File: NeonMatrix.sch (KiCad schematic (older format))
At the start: 0 parts

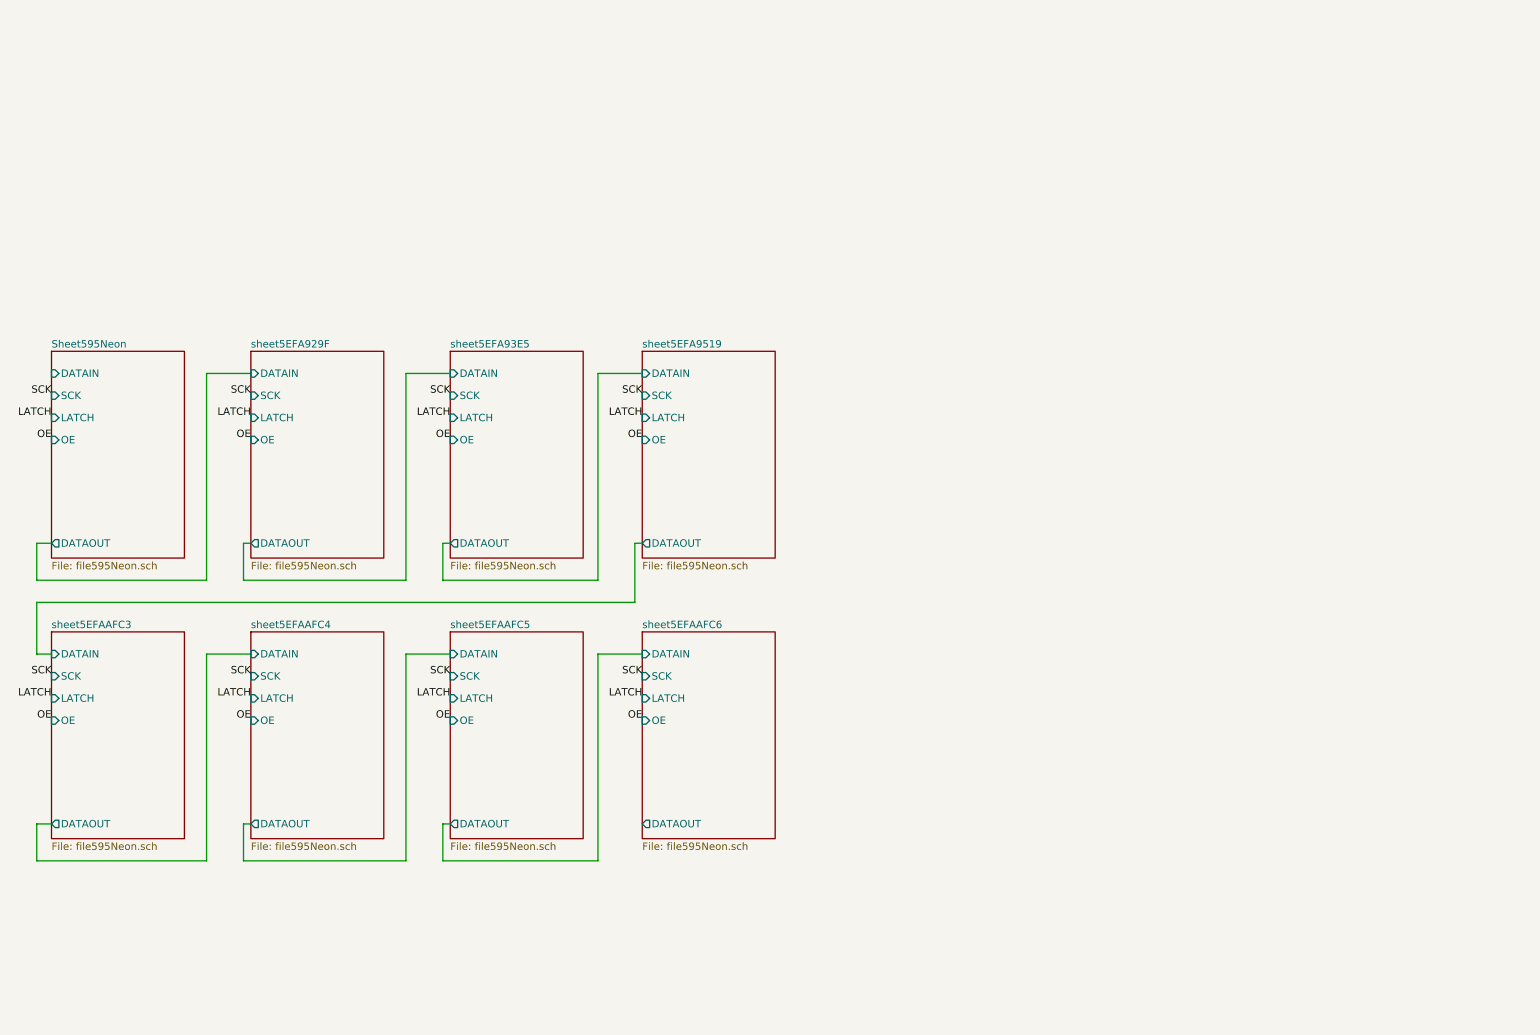
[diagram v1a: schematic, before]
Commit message: Add isolation
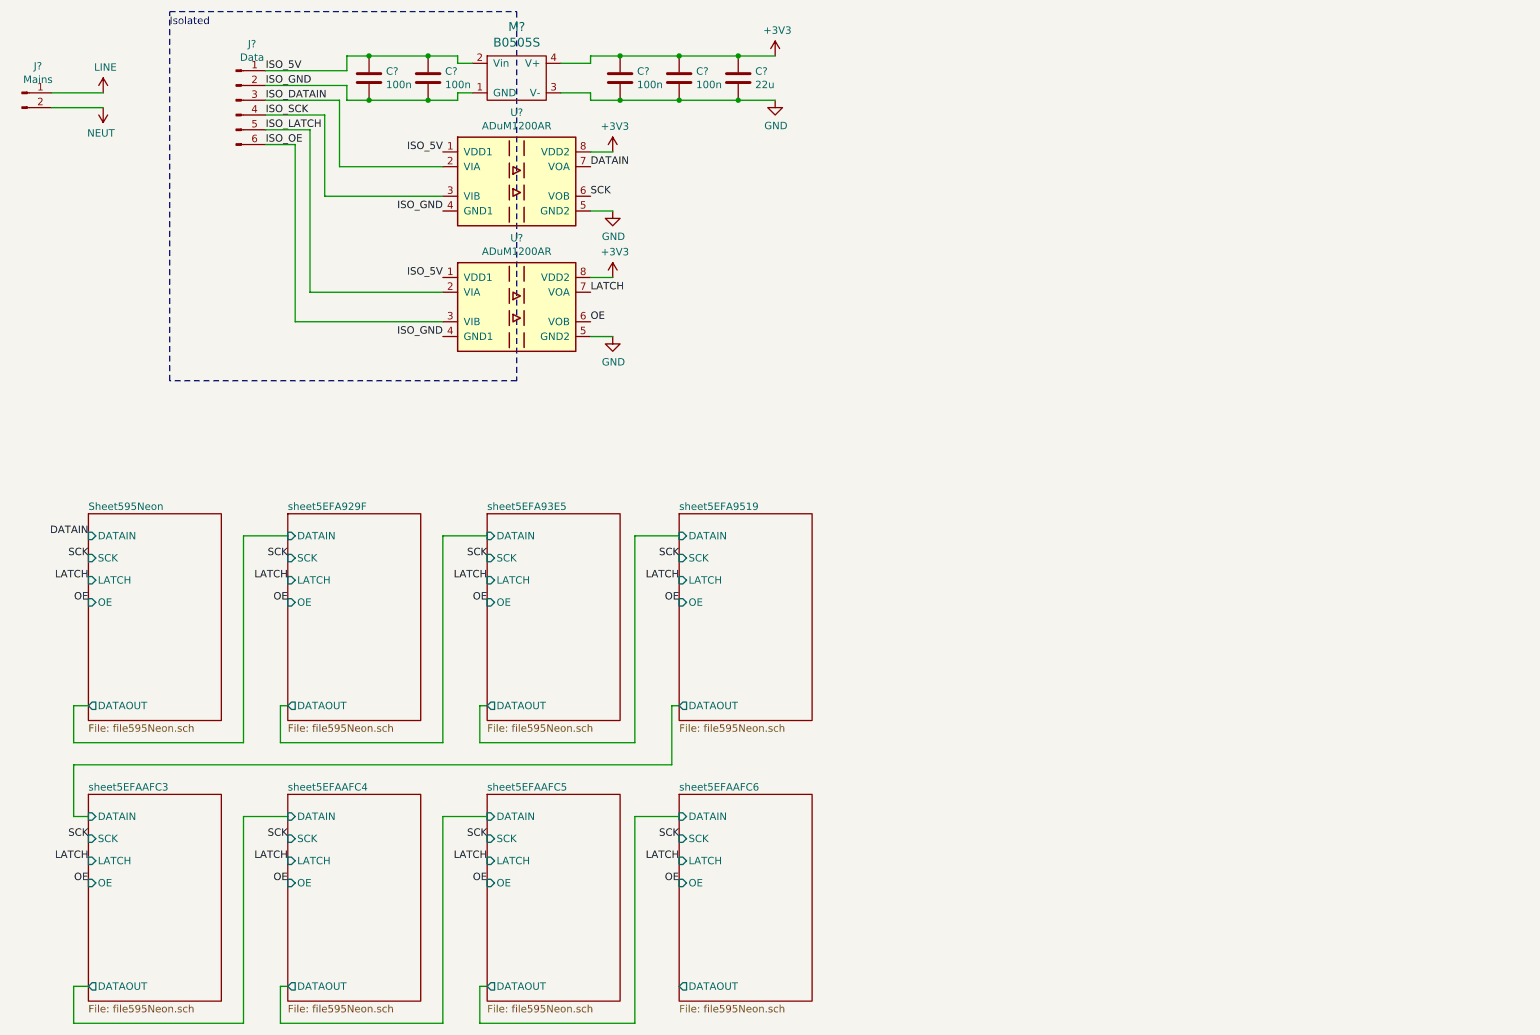
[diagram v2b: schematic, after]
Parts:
- added C? (x4): 100n, Capacitor_SMD:C_0805_2012Metric, symbol Device:C
- added C?: 22u, Capacitor_SMD:C_0805_2012Metric, symbol Device:C
- added J?: Mains, TerminalBlock_RND:TerminalBlock_RND_205-00001_1x02_P5.00mm_Horizontal, symbol Connector:Conn_01x02_Male
- added J?: Data, Connector_PinHeader_2.54mm:PinHeader_1x06_P2.54mm_Vertical, symbol Connector:Conn_01x06_Male
- added M?: B0505S, NeonMatrix:M_DCDC_SIP4, symbol NeonMatrix:B0505S
- added U? (x2): ADuM1200AR, Package_SO:SOIC-8_3.9x4.9mm_P1.27mm, symbol Isolator:ADuM1200AR
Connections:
- net LATCH: now also U?.7 (VOA)
- net OE: now also U?.6 (VOB)
- net SCK: now also U?.6 (VOB)
- new net +3V3: C?.1, C?.1, C?.1, M?.4 (V+), U?.8 (VDD2), U?.8 (VDD2)
- new net DATAIN: U?.7 (VOA)
- new net GND: C?.2, C?.2, C?.2, M?.3 (V-), U?.5 (GND2), U?.5 (GND2)
- new net ISO_5V: C?.1, C?.1, J?.1 (Pin_1), M?.2 (Vin), U?.1 (VDD1), U?.1 (VDD1)
- new net ISO_DATAIN: J?.3 (Pin_3), U?.2 (VIA)
- new net ISO_GND: C?.2, C?.2, J?.2 (Pin_2), M?.1 (GND), U?.4 (GND1), U?.4 (GND1)
- new net ISO_LATCH: J?.5 (Pin_5), U?.2 (VIA)
- new net ISO_OE: J?.6 (Pin_6), U?.3 (VIB)
- new net ISO_SCK: J?.4 (Pin_4), U?.3 (VIB)
- new net LINE: J?.1 (Pin_1)
- new net NEUT: J?.2 (Pin_2)
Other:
- note added: "Isolated"

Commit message: Add routing
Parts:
- gave numbers to parts that had none: 10
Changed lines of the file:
@@
 	1200 6050 1300 6050
 $Comp
-L Connector:Conn_01x02_Male J?
+L Connector:Conn_01x02_Male J1
 U 1 1 5EF252E6
 P 850 1150
-F 0 "J?" H 958 1331 50  0000 C CNN
+F 0 "J1" H 958 1331 50  0000 C CNN
 F 1 "Mains" H 958 1240 50  0000 C CNN
 F 2 "TerminalBlock_RND:TerminalBlock_RND_205-00001_1x02_P5.00mm_Horizontal" H 850 1150 50  0001 C CNN
@@
 $EndComp
 $Comp
-L power:LINE #PWR?
+L power:LINE #PWR0269
 U 1 1 5EF25E29
 P 1400 1150
-F 0 "#PWR?" H 1400 1000 50  0001 C CNN
+F 0 "#PWR0269" H 1400 1000 50  0001 C CNN
 F 1 "LINE" H 1415 1323 50  0000 C CNN
 F 2 "" H 1400 1150 50  0001 C CNN
@@
 $EndComp
 $Comp
-L power:NEUT #PWR?
+L power:NEUT #PWR0270
 U 1 1 5EF26410
 P 1400 1250
-F 0 "#PWR?" H 1400 1100 50  0001 C CNN
+F 0 "#PWR0270" H 1400 1100 50  0001 C CNN
 F 1 "NEUT" H 1415 1423 50  0000 C CNN
 F 2 "" H 1400 1250 50  0001 C CNN
@@
 	1400 1250 1050 1250
 $Comp
-L Connector:Conn_01x06_Male J?
+L Connector:Conn_01x06_Male J2
 U 1 1 5EF289F0
 P 2300 1200
-F 0 "J?" H 2408 1581 50  0000 C CNN
+F 0 "J2" H 2408 1581 50  0000 C CNN
 F 1 "Data" H 2408 1490 50  0000 C CNN
 F 2 "Connector_PinHeader_2.54mm:PinHeader_1x06_P2.54mm_Vertical" H 2300 1200 50  0001 C CNN
@@
 $EndComp
 $Comp
-L NeonMatrix:B0505S M?
+L NeonMatrix:B0505S M1
 U 1 1 5EF2D5C5
 P 4200 1050
-F 0 "M?" H 4200 1397 60  0000 C CNN
+F 0 "M1" H 4200 1397 60  0000 C CNN
 F 1 "B0505S" H 4200 1291 60  0000 C CNN
 F 2 "NeonMatrix:M_DCDC_SIP4" H 4200 1050 60  0001 C CNN
@@
 	2500 1100 3050 1100
 $Comp
-L Isolator:ADuM1200AR U?
+L Isolator:ADuM1200AR U9
 U 1 1 5EF33638
 P 4200 1750
-F 0 "U?" H 4200 2217 50  0000 C CNN
+F 0 "U9" H 4200 2217 50  0000 C CNN
 F 1 "ADuM1200AR" H 4200 2126 50  0000 C CNN
 F 2 "Package_SO:SOIC-8_3.9x4.9mm_P1.27mm" H 4200 1350 50  0001 C CIN
@@
 $EndComp
 $Comp
-L Isolator:ADuM1200AR U?
+L Isolator:ADuM1200AR U10
 U 1 1 5EF3D01E
 P 4200 2600
-F 0 "U?" H 4200 3067 50  0000 C CNN
+F 0 "U10" H 4200 3067 50  0000 C CNN
 F 1 "ADuM1200AR" H 4200 2976 50  0000 C CNN
 F 2 "Package_SO:SOIC-8_3.9x4.9mm_P1.27mm" H 4200 2200 50  0001 C CIN
@@
 ISO_OE
 $Comp
-L power:+3V3 #PWR?
+L power:+3V3 #PWR0271
 U 1 1 5EF5670B
 P 5950 900
-F 0 "#PWR?" H 5950 750 50  0001 C CNN
+F 0 "#PWR0271" H 5950 750 50  0001 C CNN
 F 1 "+3V3" H 5965 1073 50  0000 C CNN
 F 2 "" H 5950 900 50  0001 C CNN
@@
 $EndComp
 $Comp
-L power:GND #PWR?
+L power:GND #PWR0272
 U 1 1 5EF56B42
 P 5950 1200
-F 0 "#PWR?" H 5950 950 50  0001 C CNN
+F 0 "#PWR0272" H 5950 950 50  0001 C CNN
 F 1 "GND" H 5955 1027 50  0000 C CNN
 F 2 "" H 5950 1200 50  0001 C CNN
@@
 $EndComp
 $Comp
-L Device:C C?
+L Device:C C1
 U 1 1 5EF5D2D3
 P 3200 1050
-F 0 "C?" H 3315 1096 50  0000 L CNN
+F 0 "C1" H 3315 1096 50  0000 L CNN
 F 1 "100n" H 3315 1005 50  0000 L CNN
 F 2 "Capacitor_SMD:C_0805_2012Metric" H 3238 900 50  0001 C CNN
@@
 $EndComp
 $Comp
-L Device:C C?
+L Device:C C2
 U 1 1 5EF5E43E
 P 3600 1050
-F 0 "C?" H 3715 1096 50  0000 L CNN
+F 0 "C2" H 3715 1096 50  0000 L CNN
 F 1 "100n" H 3715 1005 50  0000 L CNN
 F 2 "Capacitor_SMD:C_0805_2012Metric" H 3638 900 50  0001 C CNN
@@
 $EndComp
 $Comp
-L Device:C C?
+L Device:C C3
 U 1 1 5EF60A70
 P 4900 1050
-F 0 "C?" H 5015 1096 50  0000 L CNN
+F 0 "C3" H 5015 1096 50  0000 L CNN
 F 1 "100n" H 5015 1005 50  0000 L CNN
 F 2 "Capacitor_SMD:C_0805_2012Metric" H 4938 900 50  0001 C CNN
@@
 	4700 900  4900 900
 $Comp
-L power:+3V3 #PWR?
+L power:+3V3 #PWR0273
 U 1 1 5EF80809
 P 4850 1550
-F 0 "#PWR?" H 4850 1400 50  0001 C CNN
+F 0 "#PWR0273" H 4850 1400 50  0001 C CNN
 F 1 "+3V3" H 4865 1723 50  0000 C CNN
 F 2 "" H 4850 1550 50  0001 C CNN
@@
 $EndComp
 $Comp
-L power:+3V3 #PWR?
+L power:+3V3 #PWR0274
 U 1 1 5EF80E8F
 P 4850 2400
-F 0 "#PWR?" H 4850 2250 50  0001 C CNN
+F 0 "#PWR0274" H 4850 2250 50  0001 C CNN
 F 1 "+3V3" H 4865 2573 50  0000 C CNN
 F 2 "" H 4850 2400 50  0001 C CNN
@@
 $EndComp
 $Comp
-L Device:C C?
+L Device:C C4
 U 1 1 5EF888A6
 P 5300 1050
-F 0 "C?" H 5415 1096 50  0000 L CNN
+F 0 "C4" H 5415 1096 50  0000 L CNN
 F 1 "100n" H 5415 1005 50  0000 L CNN
 F 2 "Capacitor_SMD:C_0805_2012Metric" H 5338 900 50  0001 C CNN
@@
 	5300 1200 5700 1200
 $Comp
-L power:GND #PWR?
+L power:GND #PWR0275
 U 1 1 5EF8F4F0
 P 4850 2800
-F 0 "#PWR?" H 4850 2550 50  0001 C CNN
+F 0 "#PWR0275" H 4850 2550 50  0001 C CNN
 F 1 "GND" H 4855 2627 50  0000 C CNN
 F 2 "" H 4850 2800 50  0001 C CNN
@@
 $EndComp
 $Comp
-L power:GND #PWR?
+L power:GND #PWR0276
 U 1 1 5EF90F2B
 P 4850 1950
-F 0 "#PWR?" H 4850 1700 50  0001 C CNN
+F 0 "#PWR0276" H 4850 1700 50  0001 C CNN
 F 1 "GND" H 4855 1777 50  0000 C CNN
 F 2 "" H 4850 1950 50  0001 C CNN
@@
 OE
 $Comp
-L Device:C C?
+L Device:C C5
 U 1 1 5EFA144C
 P 5700 1050
-F 0 "C?" H 5815 1096 50  0000 L CNN
+F 0 "C5" H 5815 1096 50  0000 L CNN
 F 1 "22u" H 5815 1005 50  0000 L CNN
 F 2 "Capacitor_SMD:C_0805_2012Metric" H 5738 900 50  0001 C CNN

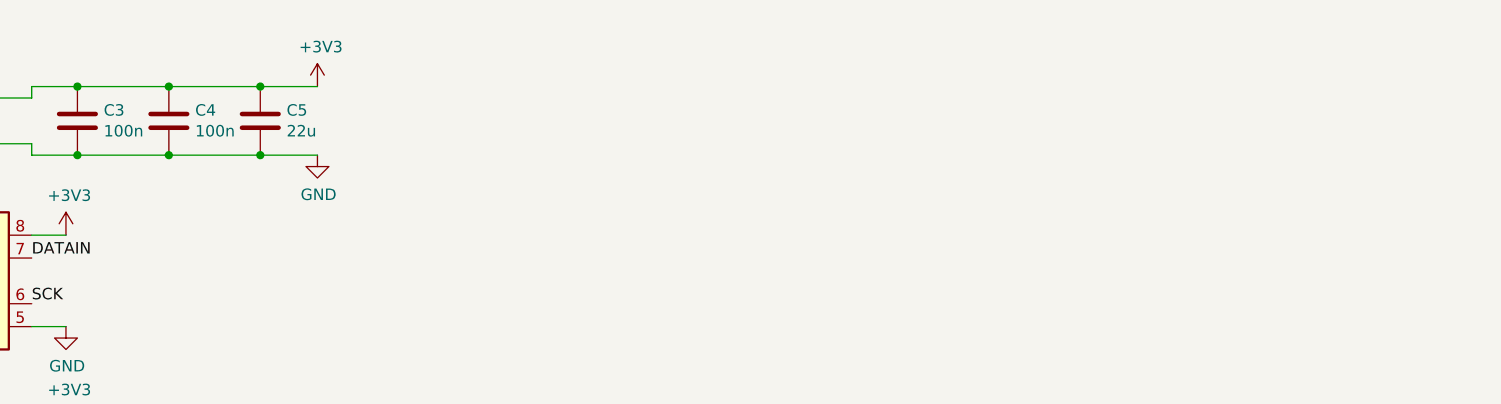
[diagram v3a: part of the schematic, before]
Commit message: Add PCB markings
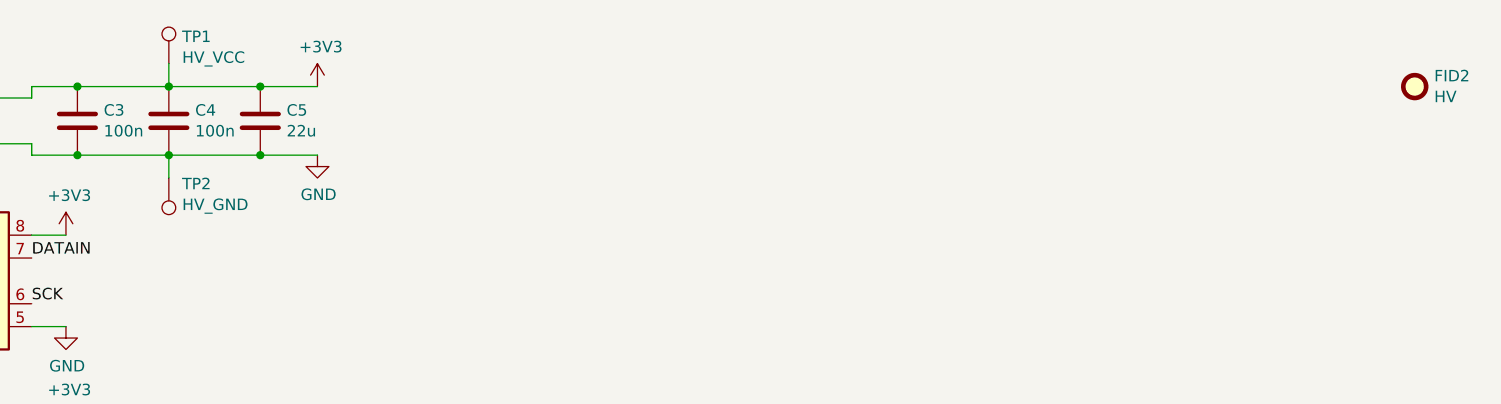
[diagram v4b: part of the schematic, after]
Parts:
- added FID2: HV, Symbol:Symbol_HighVoltage_Type1_CopperTop_Big, symbol Mechanical:Fiducial
- added TP1: HV_VCC, TestPoint:TestPoint_Pad_2.0x2.0mm, symbol Connector:TestPoint
- added TP2: HV_GND, TestPoint:TestPoint_Pad_2.0x2.0mm, symbol Connector:TestPoint
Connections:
- net +3V3: now also TP1.1
- net GND: now also TP2.1
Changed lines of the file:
@@
 Wire Wire Line
 	4500 950  4700 950
-Wire Wire Line
-	4700 900  4900 900
 $Comp
 L power:+3V3 #PWR0273
@@
 Wire Wire Line
 	5700 1200 5950 1200
+$Comp
+L Mechanical:Fiducial FID2
+U 1 1 5EF2A5C0
+P 10750 900
+F 0 "FID2" H 10835 946 50  0000 L CNN
+F 1 "HV" H 10835 855 50  0000 L CNN
+F 2 "Symbol:Symbol_HighVoltage_Type1_CopperTop_Big" H 10750 900 50  0001 C CNN
+F 3 "~" H 10750 900 50  0001 C CNN
+	1    10750 900
+	1    0    0    -1
+$EndComp
+$Comp
+L Connector:TestPoint TP1
+U 1 1 5EF2C852
+P 5300 800
+F 0 "TP1" H 5358 918 50  0000 L CNN
+F 1 "HV_VCC" H 5358 827 50  0000 L CNN
+F 2 "TestPoint:TestPoint_Pad_2.0x2.0mm" H 5500 800 50  0001 C CNN
+F 3 "~" H 5500 800 50  0001 C CNN
+	1    5300 800
+	1    0    0    -1
+$EndComp
+$Comp
+L Connector:TestPoint TP2
+U 1 1 5EF39EDF
+P 5300 1300
+F 0 "TP2" H 5242 1326 50  0000 R CNN
+F 1 "HV_GND" H 5242 1417 50  0000 R CNN
+F 2 "TestPoint:TestPoint_Pad_2.0x2.0mm" H 5500 1300 50  0001 C CNN
+F 3 "~" H 5500 1300 50  0001 C CNN
+	1    5300 1300
+	-1   0    0    1
+$EndComp
+Wire Wire Line
+	4700 900  4900 900
+Wire Wire Line
+	5300 800  5300 900
+Wire Wire Line
+	5300 1300 5300 1200
 $EndSCHEMATC

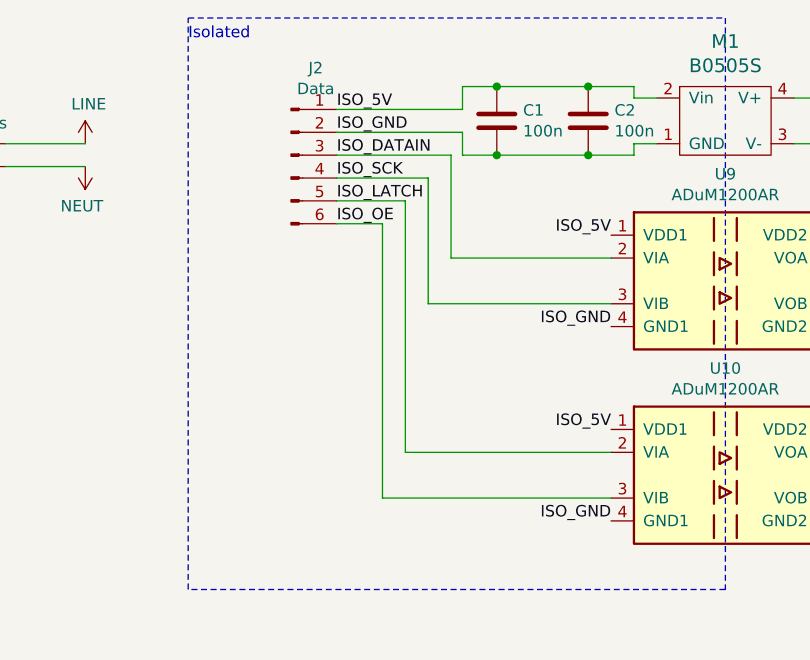
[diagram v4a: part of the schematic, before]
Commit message: Add bulk capacitance, fix isolation, silkscreen and vias
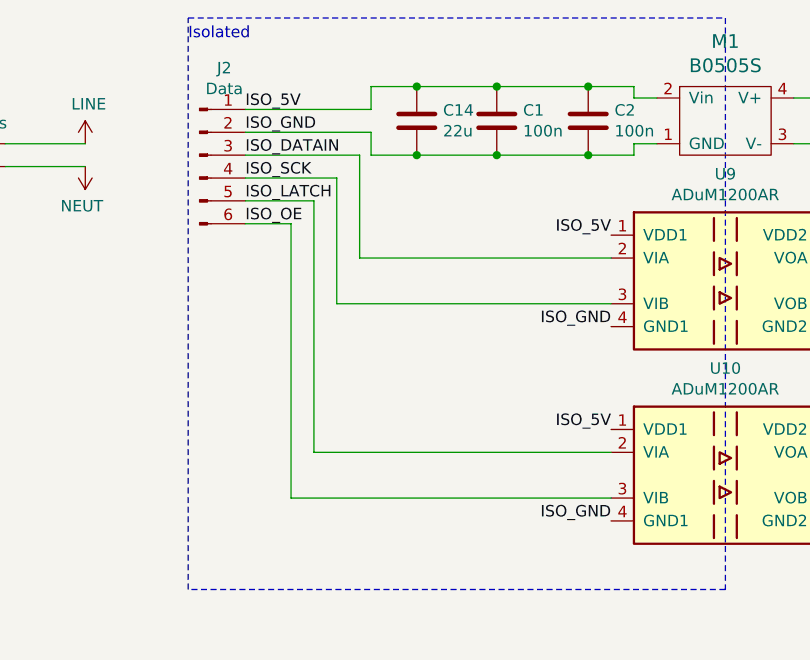
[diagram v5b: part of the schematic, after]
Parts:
- added C14: 22u, Capacitor_SMD:C_0805_2012Metric, symbol Device:C
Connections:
- net ISO_5V: now also C14.1
- net ISO_GND: now also C14.2
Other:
- moved on the sheet: J2
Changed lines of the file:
@@
 L Connector:Conn_01x06_Male J2
 U 1 1 5EF289F0
-P 2300 1200
-F 0 "J2" H 2408 1581 50  0000 C CNN
-F 1 "Data" H 2408 1490 50  0000 C CNN
-F 2 "Connector_PinHeader_2.54mm:PinHeader_1x06_P2.54mm_Vertical" H 2300 1200 50  0001 C CNN
-F 3 "~" H 2300 1200 50  0001 C CNN
-	1    2300 1200
+P 1900 1200
+F 0 "J2" H 2008 1581 50  0000 C CNN
+F 1 "Data" H 2008 1490 50  0000 C CNN
+F 2 "Connector_PinHeader_2.54mm:PinHeader_1x06_P2.54mm_Vertical" H 1900 1200 50  0001 C CNN
+F 3 "~" H 1900 1200 50  0001 C CNN
+	1    1900 1200
 	1    0    0    -1
 $EndComp
@@
 $EndComp
 Wire Wire Line
-	2500 1100 3050 1100
+	2100 1100 2650 1100
 $Comp
 L Isolator:ADuM1200AR U9
@@
 $EndComp
 Wire Wire Line
-	2500 1200 3000 1200
-Wire Wire Line
-	3000 1200 3000 1650
-Wire Wire Line
-	3000 1650 3700 1650
-Wire Wire Line
-	2500 1300 2900 1300
-Wire Wire Line
-	2900 1300 2900 1850
-Wire Wire Line
-	2900 1850 3700 1850
+	2100 1200 2600 1200
+Wire Wire Line
+	2600 1200 2600 1650
+Wire Wire Line
+	2100 1300 2500 1300
+Wire Wire Line
+	2500 1300 2500 1850
 Text Label 3700 1550 2    50   ~ 0
 ISO_5V
@@
 ISO_GND
 Wire Wire Line
-	2500 1400 2800 1400
-Wire Wire Line
-	2800 1400 2800 2500
-Wire Wire Line
-	2800 2500 3700 2500
-Wire Wire Line
-	2500 1500 2700 1500
-Wire Wire Line
-	2700 1500 2700 2700
-Wire Wire Line
-	2700 2700 3700 2700
-Text Label 2500 1000 0    50   ~ 0
+	2100 1400 2400 1400
+Wire Wire Line
+	2400 1400 2400 2500
+Wire Wire Line
+	2100 1500 2300 1500
+Wire Wire Line
+	2300 1500 2300 2700
+Text Label 2100 1000 0    50   ~ 0
 ISO_5V
-Text Label 2500 1100 0    50   ~ 0
+Text Label 2100 1100 0    50   ~ 0
 ISO_GND
 Wire Notes Line
@@
 Text Notes 1850 700  0    50   ~ 0
 Isolated
-Text Label 2500 1200 0    50   ~ 0
+Text Label 2100 1200 0    50   ~ 0
 ISO_DATAIN
-Text Label 2500 1300 0    50   ~ 0
+Text Label 2100 1300 0    50   ~ 0
 ISO_SCK
-Text Label 2500 1400 0    50   ~ 0
+Text Label 2100 1400 0    50   ~ 0
 ISO_LATCH
-Text Label 2500 1500 0    50   ~ 0
+Text Label 2100 1500 0    50   ~ 0
 ISO_OE
 $Comp
@@
 Wire Wire Line
 	3800 1150 3900 1150
-Connection ~ 3200 1200
 Wire Wire Line
 	3200 1200 3600 1200
@@
 Wire Wire Line
 	3800 900  3600 900
-Connection ~ 3200 900
 Connection ~ 3600 900
 Wire Wire Line
 	3600 900  3200 900
 Wire Wire Line
-	3050 900  3050 1000
-Wire Wire Line
-	3050 1000 2500 1000
-Wire Wire Line
-	3050 1100 3050 1200
-Wire Wire Line
-	3050 1200 3200 1200
-Wire Wire Line
-	3050 900  3200 900
+	2650 900  2650 1000
+Wire Wire Line
+	2650 1000 2100 1000
+Wire Wire Line
+	2650 1100 2650 1200
 Wire Wire Line
 	4700 1150 4700 1200
@@
 Wire Wire Line
 	5300 1300 5300 1200
+$Comp
+L Device:C C14
+U 1 1 5EF36675
+P 2850 1050
+F 0 "C14" H 2965 1096 50  0000 L CNN
+F 1 "22u" H 2965 1005 50  0000 L CNN
+F 2 "Capacitor_SMD:C_0805_2012Metric" H 2888 900 50  0001 C CNN
+F 3 "~" H 2850 1050 50  0001 C CNN
+F 4 "C45783" H 2850 1050 50  0001 C CNN "LCSC"
+	1    2850 1050
+	1    0    0    -1
+$EndComp
+Wire Wire Line
+	2650 900  2850 900
+Connection ~ 3200 900
+Connection ~ 2850 900
+Wire Wire Line
+	2850 900  3200 900
+Wire Wire Line
+	2650 1200 2850 1200
+Connection ~ 3200 1200
+Connection ~ 2850 1200
+Wire Wire Line
+	2850 1200 3200 1200
+Wire Wire Line
+	2600 1650 3700 1650
+Wire Wire Line
+	2500 1850 3700 1850
+Wire Wire Line
+	2400 2500 3700 2500
+Wire Wire Line
+	2300 2700 3700 2700
 $EndSCHEMATC
